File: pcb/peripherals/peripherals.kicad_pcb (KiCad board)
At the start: 2 copper layers, 130 parts, among them J101 Conn_01x04, J102 Conn_01x04, J103 Conn_01x04, J104 Conn_01x04, J105 Conn_01x04, J106 Conn_01x04, J107 Conn_01x04, J108 Conn_01x04, Q201 RQ3E100BNTB, Q202 RQ3E100BNTB, Q301 RQ3E100BNTB, Q302 RQ3E100BNTB, Q401 RQ3E100BNTB, Q402 RQ3E100BNTB, Q501 RQ3E100BNTB, Q502 RQ3E100BNTB, Q601 RQ3E100BNTB, Q602 RQ3E100BNTB, Q701 RQ3E100BNTB, Q702 RQ3E100BNTB, Q801 RQ3E100BNTB, Q802 RQ3E100BNTB, Q901 RQ3E100BNTB, Q902 RQ3E100BNTB, U201 DGD0506A, U301 DGD0506A, U401 DGD0506A, U501 DGD0506A, U601 DGD0506A, U701 DGD0506A, U801 DGD0506A, U901 DGD0506A

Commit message: python tile_pcb.py peripherals.kicad_pcb 3 2,4-9 0.0 30.0
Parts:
- moved C806 292.8 mm to (59.5, 236.4), turned to 270 degrees
- moved C804 292.5 mm to (66.2, 224.5)
- moved C805 292.2 mm to (60.9, 236.4), turned to 270 degrees
- moved U901 267.9 mm to (65.7, 267.9)
- moved R902 266.1 mm to (65.6, 270.5), turned to 180 degrees
- moved C901 265.4 mm to (72.1, 267.5), turned to 270 degrees
- moved L901 263.3 mm to (77.1, 265.0)
- moved C906 262.9 mm to (59.5, 266.4), turned to 270 degrees
- moved C904 262.8 mm to (66.2, 254.5)
- moved C902 262.5 mm to (65.7, 265.1)
- moved C905 262.3 mm to (60.9, 266.4), turned to 270 degrees
- moved Q902 260.4 mm to (54.1, 268.6), turned to 90 degrees
- moved TP902 257.2 mm to (54.0, 265.2)
- moved R903 257.1 mm to (58.1, 269.8), turned to 180 degrees
- moved TP901 256.5 mm to (57.7, 265.4)
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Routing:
- net Net-(R401-Pad2): track 0.00 -> 21.4 mm
- net Net-(R201-Pad2): track 0.00 -> 21.4 mm
- net Net-(R801-Pad2): track 0.00 -> 21.4 mm
- net Net-(R701-Pad2): track 0.00 -> 21.4 mm
- net Net-(R601-Pad2): track 0.00 -> 21.4 mm
- net Net-(R501-Pad2): track 0.00 -> 21.4 mm
- net Net-(R901-Pad2): track 0.00 -> 21.4 mm

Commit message: Save before debugging weird netlist buggery
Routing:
- net Net-(R201-Pad2): track 21.4 -> 7.42 mm
- net /Sheet5B7230C3/OUT: track 0.00 -> 8.64 mm
- net Net-(C301-Pad1): track 0.00 -> 6.60 mm
- net Net-(R202-Pad1): track 0.00 -> 2.51 mm
- net Net-(C201-Pad1): track 0.00 -> 2.29 mm
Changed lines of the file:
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@@
     (thickness 1.6)
     (drawings 1)
-    (tracks 110)
+    (tracks 117)
     (zones 0)
     (modules 130)
@@
     (effects (font (size 2.54 2.54) (thickness 0.254)) (justify left))
   )
+  (segment (start 60.55 87.35) (end 60.9 87) (width 0.254) (layer F.Cu) (net 1))
+  (segment (start 59.5 87.35) (end 60.55 87.35) (width 0.254) (layer F.Cu) (net 1))
+  (segment (start 54.425 83.804) (end 54.425 83.25) (width 0.254) (layer F.Cu) (net 1))
+  (segment (start 57.971 87.35) (end 54.425 83.804) (width 0.254) (layer F.Cu) (net 1))
+  (segment (start 59.5 87.35) (end 57.971 87.35) (width 0.254) (layer F.Cu) (net 1))
+  (segment (start 64.546 55.1) (end 63.725 55.921) (width 0.254) (layer F.Cu) (net 27))
+  (segment (start 63.725 55.921) (end 63.725 56.868999) (width 0.254) (layer F.Cu) (net 27))
+  (segment (start 65.1 55.1) (end 64.546 55.1) (width 0.254) (layer F.Cu) (net 27))
+  (segment (start 75.05 55.7) (end 75.75 55) (width 0.254) (layer F.Cu) (net 27))
+  (segment (start 72.1 55.7) (end 75.05 55.7) (width 0.254) (layer F.Cu) (net 27))
   (segment (start 59.65 53.1) (end 59.5 53.1) (width 0.1524) (layer F.Cu) (net 29))
   (segment (start 61.480201 54.930201) (end 59.65 53.1) (width 0.1524) (layer F.Cu) (net 29))
@@
   (segment (start 62.8976 267.9) (end 61.480201 266.482601) (width 0.1524) (layer F.Cu) (net 72))
   (segment (start 63.725 267.9) (end 62.8976 267.9) (width 0.1524) (layer F.Cu) (net 72))
+  (segment (start 65.1 85.604) (end 63.835001 86.868999) (width 0.254) (layer F.Cu) (net 75))
+  (segment (start 65.1 85.1) (end 65.1 85.604) (width 0.254) (layer F.Cu) (net 75))
   (segment (start 59.65 83.1) (end 59.5 83.1) (width 0.1524) (layer F.Cu) (net 77))
-  (segment (start 61.480201 84.930201) (end 59.65 83.1) (width 0.1524) (layer F.Cu) (net 77))
-  (segment (start 61.480201 86.482601) (end 61.480201 84.930201) (width 0.1524) (layer F.Cu) (net 77))
-  (segment (start 62.8976 87.9) (end 61.480201 86.482601) (width 0.1524) (layer F.Cu) (net 77))
-  (segment (start 63.725 87.9) (end 62.8976 87.9) (width 0.1524) (layer F.Cu) (net 77))
   (segment (start 59.65 83.1) (end 59.5 83.1) (width 0.1524) (layer F.Cu) (net 77))
-  (segment (start 61.480201 84.930201) (end 59.65 83.1) (width 0.1524) (layer F.Cu) (net 77))
-  (segment (start 61.480201 86.482601) (end 61.480201 84.930201) (width 0.1524) (layer F.Cu) (net 77))
-  (segment (start 62.8976 87.9) (end 61.480201 86.482601) (width 0.1524) (layer F.Cu) (net 77))
-  (segment (start 63.725 87.9) (end 62.8976 87.9) (width 0.1524) (layer F.Cu) (net 77))
   (segment (start 59.65 83.1) (end 59.5 83.1) (width 0.1524) (layer F.Cu) (net 77))
-  (segment (start 61.480201 84.930201) (end 59.65 83.1) (width 0.1524) (layer F.Cu) (net 77))
-  (segment (start 61.480201 86.482601) (end 61.480201 84.930201) (width 0.1524) (layer F.Cu) (net 77))
-  (segment (start 62.8976 87.9) (end 61.480201 86.482601) (width 0.1524) (layer F.Cu) (net 77))
   (segment (start 63.725 87.9) (end 62.8976 87.9) (width 0.1524) (layer F.Cu) (net 77))
+  (segment (start 62.8976 87.9) (end 61.480201 86.482601) (width 0.1524) (layer F.Cu) (net 77))
+  (segment (start 61.480201 86.482601) (end 61.480201 84.930201) (width 0.1524) (layer F.Cu) (net 77))
+  (segment (start 61.480201 84.930201) (end 59.65 83.1) (width 0.1524) (layer F.Cu) (net 77))
+  (segment (start 66.504 90.5) (end 67.675 89.329) (width 0.254) (layer F.Cu) (net 79))
+  (segment (start 67.675 89.329) (end 67.675 88.931001) (width 0.254) (layer F.Cu) (net 79))
+  (segment (start 66.05 90.5) (end 66.504 90.5) (width 0.254) (layer F.Cu) (net 79))
   (segment (start 59.65 143.1) (end 59.5 143.1) (width 0.1524) (layer F.Cu) (net 88))
   (segment (start 61.480201 144.930201) (end 59.65 143.1) (width 0.1524) (layer F.Cu) (net 88))

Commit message: Fix bad pad net labeling in tile_pcb.py; python tile_pcb.py peripherals.kicad_pcb 2 3-9 0.0 30.0
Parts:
- moved C306 60.0 mm to (59.5, 116.4)
- moved TP301 60.0 mm to (57.7, 115.4)
- moved U301 60.0 mm to (65.7, 117.9)
- moved C301 60.0 mm to (72.1, 117.5)
- moved C303 60.0 mm to (52.1, 100.7)
- moved C304 60.0 mm to (66.2, 104.5)
- moved C305 60.0 mm to (60.9, 116.5)
- moved L301 60.0 mm to (77.1, 115.0)
- moved Q301 60.0 mm to (54.1, 111.7)
- moved R302 60.0 mm to (65.6, 120.5)
- moved R303 60.0 mm to (58.1, 119.8)
- moved TP302 60.0 mm to (54.0, 115.2)
- moved C302 60.0 mm to (65.7, 115.1)
- moved Q302 60.0 mm to (54.1, 118.6)
- moved R301 60.0 mm to (58.4, 113.1)
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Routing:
- net Net-(R801-Pad2): track 21.4 -> 7.42 mm
- net Net-(R401-Pad2): track 21.4 -> 7.42 mm
- net Net-(R701-Pad2): track 21.4 -> 7.42 mm
- net Net-(R601-Pad2): track 21.4 -> 7.42 mm
- net Net-(R501-Pad2): track 21.4 -> 7.42 mm
- net Net-(R901-Pad2): track 21.4 -> 7.42 mm
- net Net-(C301-Pad1): track 6.60 -> 2.29 mm
- net Net-(R902-Pad1): track 0.00 -> 2.51 mm
- net Net-(R802-Pad1): track 0.00 -> 2.51 mm
- net Net-(R702-Pad1): track 0.00 -> 2.51 mm
- net Net-(R602-Pad1): track 0.00 -> 2.51 mm
- net Net-(R502-Pad1): track 0.00 -> 2.51 mm
- net Net-(R402-Pad1): track 0.00 -> 2.51 mm
- net Net-(R302-Pad1): track 0.00 -> 2.51 mm
- net Net-(C701-Pad1): track 0.00 -> 2.29 mm
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
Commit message: Save before testing auto_tile.py
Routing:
- net Net-(C205-Pad1): track 0.00 -> 6.89 mm, vias 0 -> 2

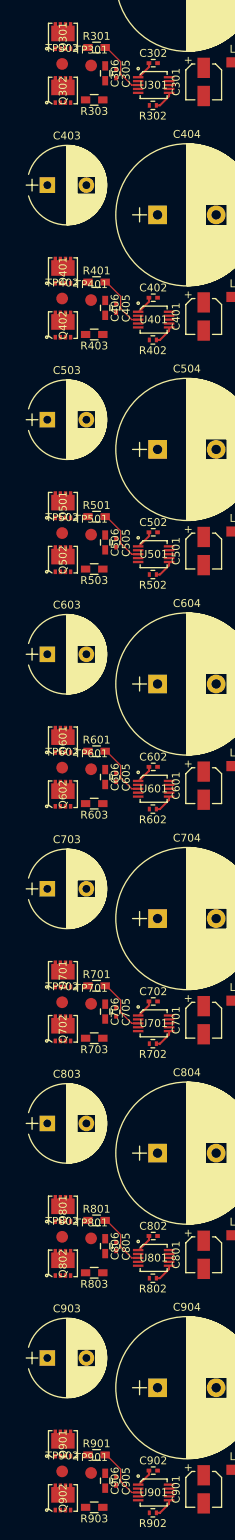
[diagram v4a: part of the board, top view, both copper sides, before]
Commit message: Autotiling probably works now, aside from breaking from the sheet stuff probably
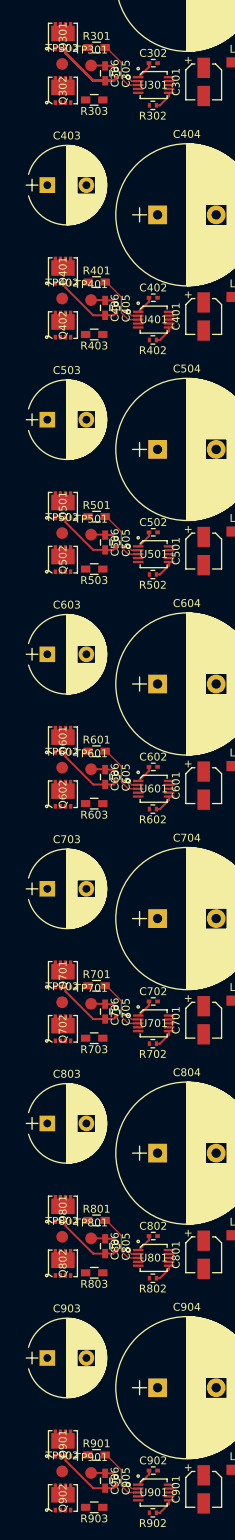
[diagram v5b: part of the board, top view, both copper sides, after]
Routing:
- net /Sheet5B7230C3/OUT: track 8.64 -> 95.1 mm
- net Net-(C905-Pad1): track 0.00 -> 6.89 mm, vias 0 -> 2
- net Net-(C805-Pad1): track 0.00 -> 6.89 mm, vias 0 -> 2
- net Net-(C705-Pad1): track 0.00 -> 6.89 mm, vias 0 -> 2
- net Net-(C605-Pad1): track 0.00 -> 6.89 mm, vias 0 -> 2
- net Net-(C505-Pad1): track 0.00 -> 6.89 mm, vias 0 -> 2
- net Net-(C405-Pad1): track 0.00 -> 6.89 mm, vias 0 -> 2
- net Net-(C305-Pad1): track 0.00 -> 6.89 mm, vias 0 -> 2

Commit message: Save before autotiling
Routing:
- net /Sheet5B7230C3/OUT: track 95.1 -> 12.1 mm
- net GND: track 0.00 -> 56.7 mm, vias 0 -> 4
- net +BATT: track 0.00 -> 33.6 mm
- net Net-(R203-Pad1): track 0.00 -> 15.1 mm
- net Net-(C201-Pad1): track 2.29 -> 14.9 mm
- net /sheet5B6E6A5D/OUT: track 0.00 -> 8.64 mm
- net /sheet5B6E6A5C/OUT: track 0.00 -> 8.64 mm
- net /sheet5B6E69B5/OUT: track 0.00 -> 8.64 mm
- net /sheet5B6E6A5B/OUT: track 0.00 -> 8.64 mm
- net /sheet5B6E6A5A/OUT: track 0.00 -> 8.64 mm
- net /sheet5B6E69C4/OUT: track 0.00 -> 8.64 mm
- net /sheet5B6E69C3/OUT: track 0.00 -> 8.64 mm
- net Net-(Q201-Pad4): track 0.00 -> 2.29 mm
- net Net-(Q202-Pad4): track 0.00 -> 2.07 mm
- net /Sheet5B7230C3/IN: track 0.00 -> 1.24 mm, vias 0 -> 1
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
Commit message: python autotile_pcb.py peripherals.kicad_pcb 2 3-9 48.3 63.8 79.9 92.7 0.0 30.0 plus some layout work
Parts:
- moved R903 257.2 mm to (122.0, 50.7), turned to 0 degrees
- moved Q902 257.0 mm to (126.0, 51.9), turned to 270 degrees
- moved R902 255.2 mm to (114.5, 50.0), turned to 0 degrees
- moved TP902 250.5 mm to (126.1, 55.3), turned to 180 degrees
- moved U901 250.1 mm to (114.4, 52.6), turned to 180 degrees
- moved C906 249.9 mm to (120.6, 54.1), turned to 90 degrees
- moved C905 249.3 mm to (119.2, 54.0), turned to 90 degrees
- moved TP901 248.9 mm to (122.4, 55.1), turned to 180 degrees
- moved C901 247.1 mm to (108.0, 53.0), turned to 90 degrees
- moved C902 244.6 mm to (114.5, 55.4), turned to 180 degrees
- moved R901 244.1 mm to (121.7, 57.4), turned to 180 degrees
- moved Q901 243.7 mm to (126.0, 58.8), turned to 270 degrees
- moved L901 240.9 mm to (103.0, 55.5), turned to 180 degrees
- moved C903 224.1 mm to (128.0, 69.8), turned to 180 degrees
- moved C904 223.6 mm to (113.9, 66.0), turned to 180 degrees
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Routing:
- net GND: track 56.7 -> 453.6 mm, vias 4 -> 32
- net +BATT: track 33.6 -> 268.8 mm
- net Net-(R903-Pad1): track 0.00 -> 15.1 mm
- net Net-(R603-Pad1): track 0.00 -> 15.1 mm
- net Net-(R303-Pad1): track 0.00 -> 15.1 mm
- net Net-(R803-Pad1): track 0.00 -> 15.1 mm
- net Net-(R703-Pad1): track 0.00 -> 15.1 mm
- net Net-(R503-Pad1): track 0.00 -> 15.1 mm
- net Net-(R403-Pad1): track 0.00 -> 15.1 mm
- net Net-(C801-Pad1): track 2.29 -> 14.9 mm
- net Net-(C901-Pad1): track 2.29 -> 14.9 mm
- net Net-(C701-Pad1): track 2.29 -> 14.9 mm
- net Net-(C601-Pad1): track 2.29 -> 14.9 mm
- net Net-(C501-Pad1): track 2.29 -> 14.9 mm
- net Net-(C401-Pad1): track 2.29 -> 14.9 mm
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
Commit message: Layout finished and Gerbers generated
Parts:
- added MH101: MountingHole, Mounting_Holes:MountingHole_5.3mm_M5_Pad, F.Cu at (42.0, 164.0)
- added MH102: MountingHole, Mounting_Holes:MountingHole_5.3mm_M5_Pad, F.Cu at (42.0, 55.5)
- added MH103: MountingHole, Mounting_Holes:MountingHole_5.3mm_M5_Pad, F.Cu at (139.2, 55.2)
- added MH104: MountingHole, Mounting_Holes:MountingHole_5.3mm_M5_Pad, F.Cu at (139.5, 164.0)
- J101, J102, J107, J108: value Conn_01x04 -> Conn_01x05; footprint Socket_Strips:Socket_Strip_Straight_1x04_Pitch2.54mm -> Socket_Strips:Socket_Strip_Straight_1x05_Pitch2.54mm
- J105, J106: moved to B.Cu
- moved J106 153.7 mm to (40.3, 111.3)
- moved J105 146.7 mm to (141.4, 102.3)
- moved J103 144.2 mm to (141.4, 102.5), turned to 180 degrees
- moved TP101 84.5 mm to (94.5, 61.1)
- moved J101 29.5 mm to (85.1, 120.8)
- moved J108 17.5 mm to (93.0, 92.5)
- moved BT101 12.6 mm to (99.2, 52.5)
- moved J102 9.03 mm to (97.3, 92.5)
- moved J107 4.56 mm to (89.2, 120.7)
- moved C601 2.68 mm to (107.6, 145.7)
- moved C602 2.68 mm to (114.0, 148.1)
- moved C604 2.68 mm to (113.5, 158.7)
- moved C701 2.68 mm to (107.6, 115.7)
- moved C704 2.68 mm to (113.5, 128.7)
- moved C705 2.68 mm to (118.8, 116.7)
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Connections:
- J101 pad 1: /sheet5B6E69C4/IN -> GND
- J101 pad 2: /sheet5B6E69C3/IN -> /sheet5B6E69C4/IN
- J101 pad 3: /sheet5B6E69B5/IN -> /sheet5B6E69C3/IN
- J101 pad 4: /Sheet5B7230C3/IN -> /sheet5B6E69B5/IN
- J102 pad 1: /sheet5B6E6A5D/IN -> GND
- J102 pad 2: /sheet5B6E6A5C/IN -> /sheet5B6E6A5D/IN
- J102 pad 3: /sheet5B6E6A5B/IN -> /sheet5B6E6A5C/IN
- J102 pad 4: /sheet5B6E6A5A/IN -> /sheet5B6E6A5B/IN
- J107 pad 1: /sheet5B6E69C4/EN -> GND
- J107 pad 2: /sheet5B6E69C3/EN -> /sheet5B6E69C4/EN
- J107 pad 3: /sheet5B6E69B5/EN -> /sheet5B6E69C3/EN
- J107 pad 4: /Sheet5B7230C3/EN -> /sheet5B6E69B5/EN
- J108 pad 1: /sheet5B6E6A5D/EN -> GND
- J108 pad 2: /sheet5B6E6A5C/EN -> /sheet5B6E6A5D/EN
- J108 pad 3: /sheet5B6E6A5B/EN -> /sheet5B6E6A5C/EN
- J108 pad 4: /sheet5B6E6A5A/EN -> /sheet5B6E6A5B/EN
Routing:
- net GND: track 453.6 -> 823.6 mm, vias 32 -> 63
- net +BATT: track 268.8 -> 418.8 mm
- net /sheet5B6E69C4/IN: track 1.24 -> 71.6 mm, vias 1 -> 2
- net /sheet5B6E69C4/EN: track 1.22 -> 68.3 mm, vias 1 -> 2
- net /sheet5B6E6A5D/EN: track 1.22 -> 65.3 mm, vias 1 -> 3
- net /sheet5B6E6A5D/IN: track 1.24 -> 62.9 mm, vias 1 -> 3
- net /sheet5B6E6A5A/IN: track 1.24 -> 55.5 mm, vias 1 -> 2
- net /sheet5B6E6A5A/EN: track 1.22 -> 55.4 mm, vias 1 -> 2
- net /Sheet5B7230C3/EN: track 1.22 -> 53.9 mm, vias 1 -> 3
- net /Sheet5B7230C3/IN: track 1.24 -> 53.6 mm, vias 1 -> 3
- net /Sheet5B7230C3/OUT: track 12.1 -> 56.1 mm
- net /sheet5B6E69C3/IN: track 1.24 -> 40.5 mm, vias 1 -> 3
- net /sheet5B6E6A5D/OUT: track 12.1 -> 51.2 mm
- net /sheet5B6E6A5C/EN: track 1.22 -> 39.8 mm, vias 1 -> 3
- net /sheet5B6E69C3/EN: track 1.22 -> 39.8 mm
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- added copper zone on F.Cu, net +BATT
- added copper zone on F.Cu, net /Sheet5B7230C3/OUT
- added copper zone on F.Cu, net /sheet5B6E69B5/OUT
- added copper zone on F.Cu, net /sheet5B6E69C3/OUT
- added copper zone on F.Cu, net /sheet5B6E69C4/OUT
- added copper zone on F.Cu, net /sheet5B6E6A5A/OUT
- added copper zone on F.Cu, net /sheet5B6E6A5B/OUT
- added copper zone on F.Cu, net /sheet5B6E6A5C/OUT
- added copper zone on F.Cu, net /sheet5B6E6A5D/OUT
- added copper zone on B.Cu, net GND
- added copper zone on F.Cu, net GND
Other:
- board outline added: 113.5 x 124.5 mm
- net class Default: clearance 0.254 -> 0.1524; trace_width 0.254 -> 0.1524
- rule trace_clearance: 0.254 -> 0.1524
